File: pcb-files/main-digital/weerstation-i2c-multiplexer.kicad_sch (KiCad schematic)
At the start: 14 parts, among them J11 rotatie as5600, J12 rotatie as5600, J13 rotatie as5600 2, J14 rotatie as5600 2, J15 rotatie as5600 2, J17 rotatie as5600 3, J18 rotatie as5600 3, J19 rotatie as5600 3, J20 rotatie as5600 4, J21 rotatie as5600 4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

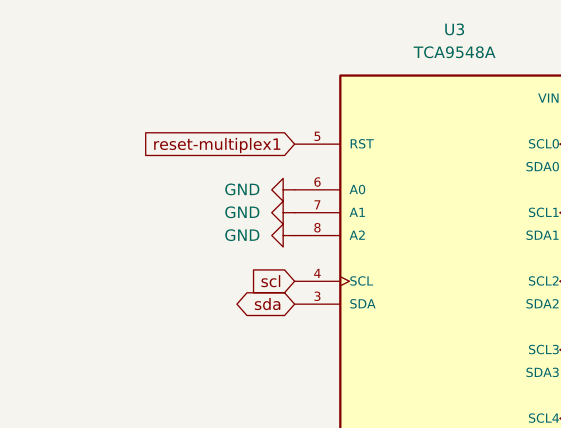
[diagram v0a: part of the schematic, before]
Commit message: update pcb files better layout and grounding inproved
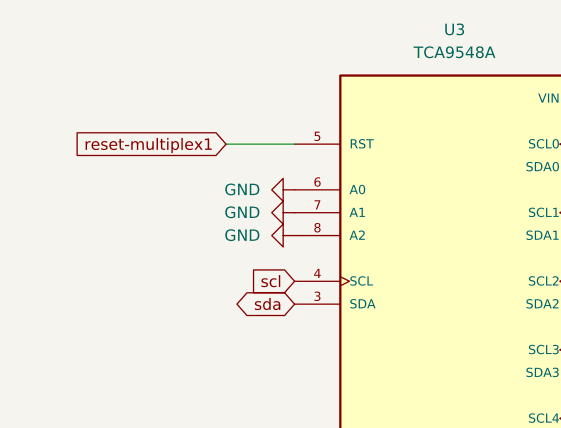
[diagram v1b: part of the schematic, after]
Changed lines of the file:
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@@
+	(wire
+		(pts
+			(xy 81.28 52.07) (xy 88.9 52.07)
+		)
+		(stroke
+			(width 0)
+			(type default)
+		)
+	)
 	(wire
 		(pts
@@
 	(global_label "reset-multiplex1"
 		(shape input)
-		(at 88.9 52.07 180)
+		(at 81.28 52.07 180)
 		(fields_autoplaced yes)
 		(effects
@@
 		)
 		(property "Intersheetrefs" "${INTERSHEET_REFS}"
-			(at 69.6468 52.07 0)
+			(at 62.0268 52.07 0)
 			(effects
 				(font
